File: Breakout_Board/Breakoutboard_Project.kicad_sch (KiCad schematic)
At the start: 14 parts, among them J1 Conn_01x17, U2 STM32F411

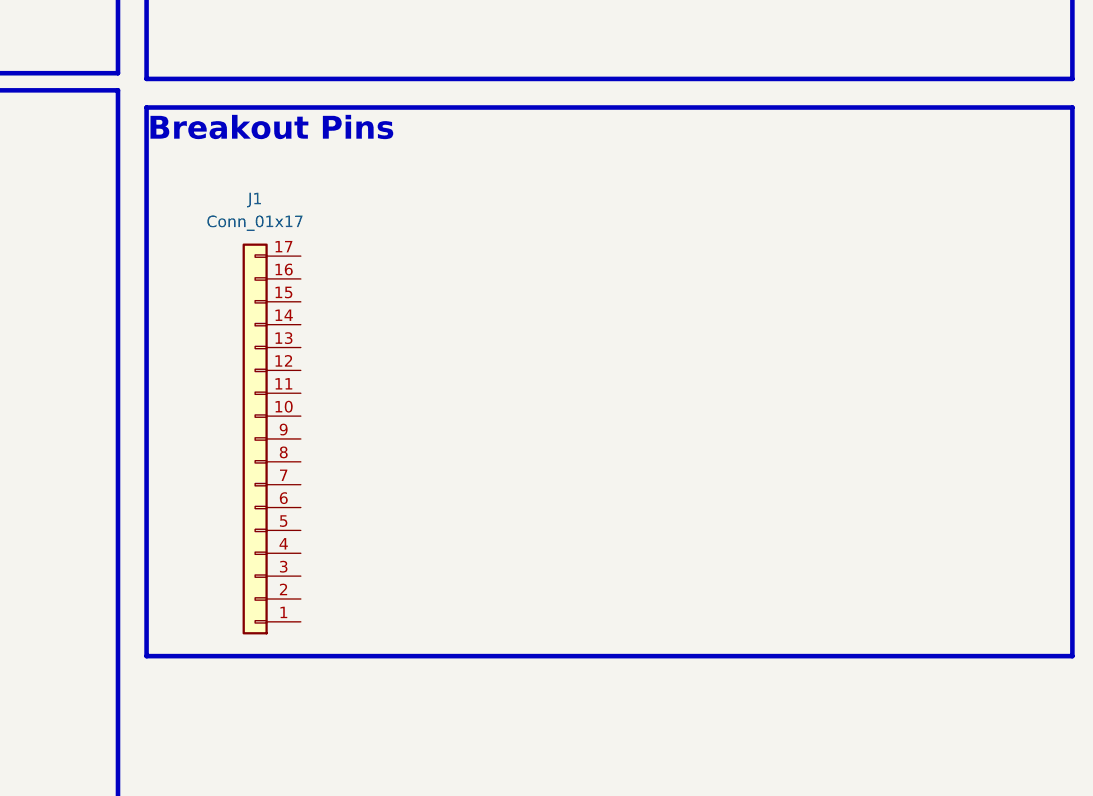
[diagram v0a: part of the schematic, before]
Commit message: Add breakout pin headers (J1-J4) for probing all sensor/MCU signals
Co-Authored-By: Claude Sonnet 5 <noreply@anthropic.com>
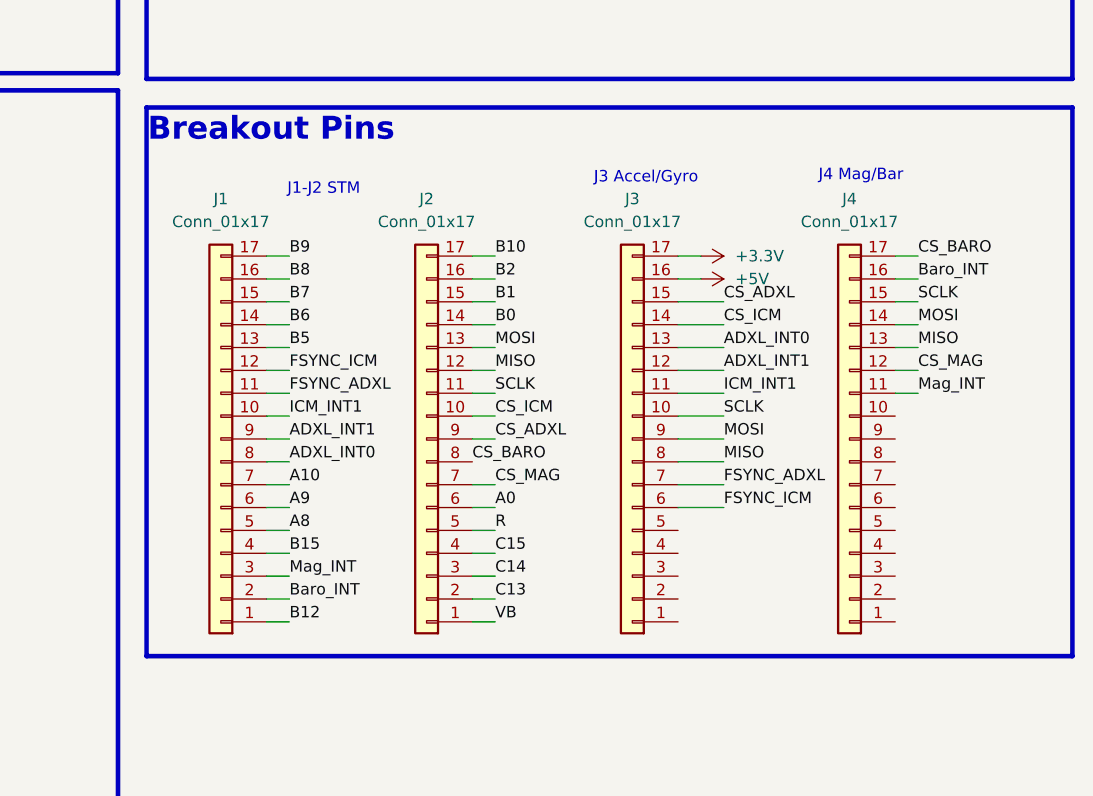
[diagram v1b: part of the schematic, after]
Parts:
- added J2, J3, J4: Conn_01x17, Package_QFP:LQFP-176_24x24mm_P0.5mm, symbol Connector_Generic:Conn_01x17
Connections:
- net +3.3V: now also J3.17 (Pin_17)
- net +5V: now also J3.16 (Pin_16)
- net A0: now also J2.6 (Pin_6)
- net A10: now also J1.7 (Pin_7)
- net A8: now also J1.5 (Pin_5)
- net A9: now also J1.6 (Pin_6)
- net ADXL_INT0: now also J1.8 (Pin_8), J3.13 (Pin_13)
- net ADXL_INT1: now also J1.9 (Pin_9), J3.12 (Pin_12)
- net B0: now also J2.14 (Pin_14)
- net B1: now also J2.15 (Pin_15)
- net B10: now also J2.17 (Pin_17)
- net B12: now also J1.1 (Pin_1)
- net B15: now also J1.4 (Pin_4)
- net B2: now also J2.16 (Pin_16)
- net B5: now also J1.13 (Pin_13)
- net B6: now also J1.14 (Pin_14)
- net B7: now also J1.15 (Pin_15)
- net B8: now also J1.16 (Pin_16)
- net B9: now also J1.17 (Pin_17)
- net Baro_INT: now also J1.2 (Pin_2), J4.16 (Pin_16)
- net C13: now also J2.2 (Pin_2)
- net C14: now also J2.3 (Pin_3)
- net C15: now also J2.4 (Pin_4)
- net CS_ADXL: now also J2.9 (Pin_9), J3.15 (Pin_15)
- net CS_BARO: now also J2.8 (Pin_8), J4.17 (Pin_17)
- net CS_ICM: now also J2.10 (Pin_10), J3.14 (Pin_14)
- net CS_MAG: now also J2.7 (Pin_7), J4.12 (Pin_12)
- net FSYNC_ADXL: now also J1.11 (Pin_11), J3.7 (Pin_7)
- net FSYNC_ICM: now also J1.12 (Pin_12), J3.6 (Pin_6)
- net ICM_INT1: now also J1.10 (Pin_10), J3.11 (Pin_11)
- net MISO: now also J2.12 (Pin_12), J3.8 (Pin_8), J4.13 (Pin_13)
- net MOSI: now also J2.13 (Pin_13), J3.9 (Pin_9), J4.14 (Pin_14)
- net Mag_INT: now also J1.3 (Pin_3), J4.11 (Pin_11)
- net R: now also J2.5 (Pin_5)
- net SCLK: now also J2.11 (Pin_11), J3.10 (Pin_10), J4.15 (Pin_15)
- net VB: now also J2.1 (Pin_1)
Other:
- note added: "J1-J2 STM"
- note added: "J3 Accel/Gyro"
- note added: "J4 Mag/Bar"
- moved on the sheet: J1
